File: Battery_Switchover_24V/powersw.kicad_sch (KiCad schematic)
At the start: 39 parts, among them J10 ATX_2X3, J11 ATX_2X3, J12 ATX_2X3, J13 ATX_2X3, J2 M8, J4 M8, J5 M8, J8 ATX_2X3, J9 ATX_2X3, Q10 FDBL86066-F085, Q4 FDBL86066-F085, Q5 FDBL86066-F085, Q6 FDBL86066-F085, Q7 FDBL86066-F085, Q8 FDBL86066-F085, Q9 FDBL86066-F085, U15 IRS21867S, U16 LM74610QDGKRQ1, U17 IRS21867S, U3 IRS21867S, U6 LM74610QDGKRQ1

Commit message: Board turned to horizontal
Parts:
- C9: footprint Capacitor_SMD:C_0603_1608Metric -> Capacitor_SMD:C_1206_3216Metric
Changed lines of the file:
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@@
 			)
 		)
-		(property "Footprint" "Capacitor_SMD:C_0603_1608Metric"
+		(property "Footprint" "Capacitor_SMD:C_1206_3216Metric"
 			(at 92.71 187.96 0)
 			(effects

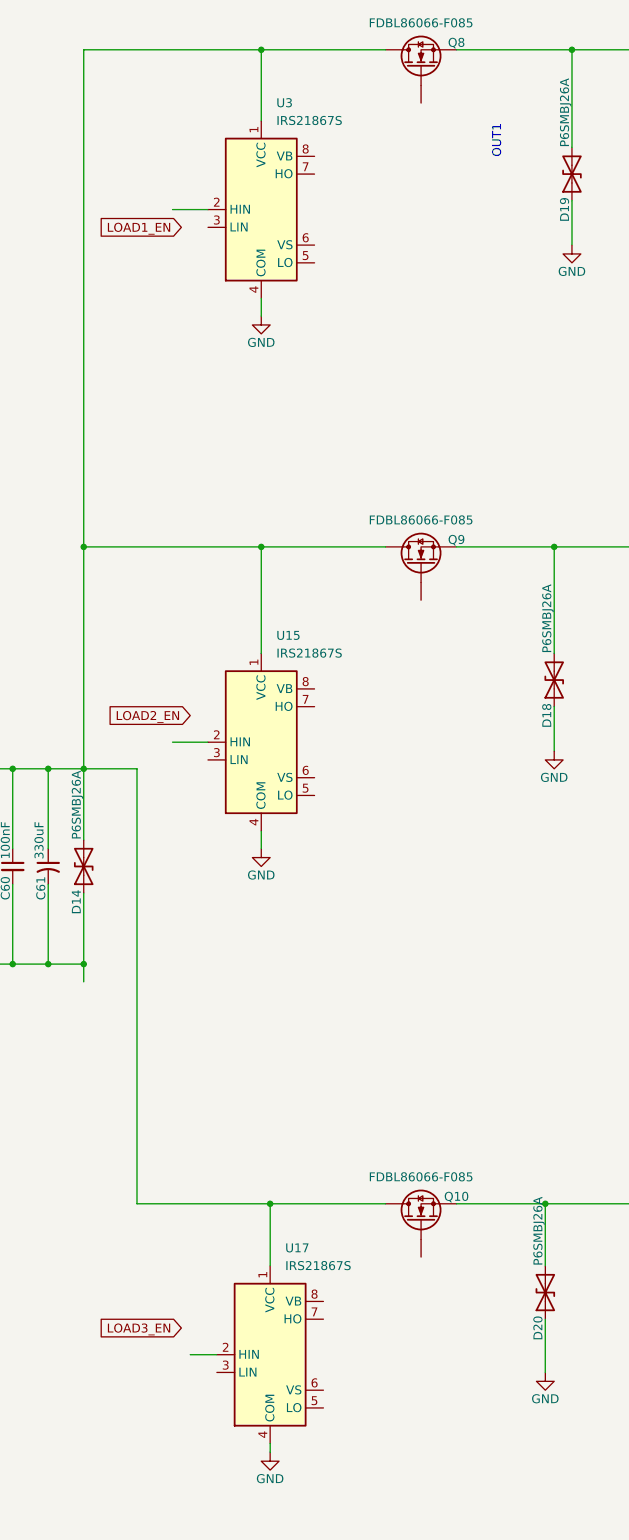
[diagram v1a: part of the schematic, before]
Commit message: hiside load switch revised
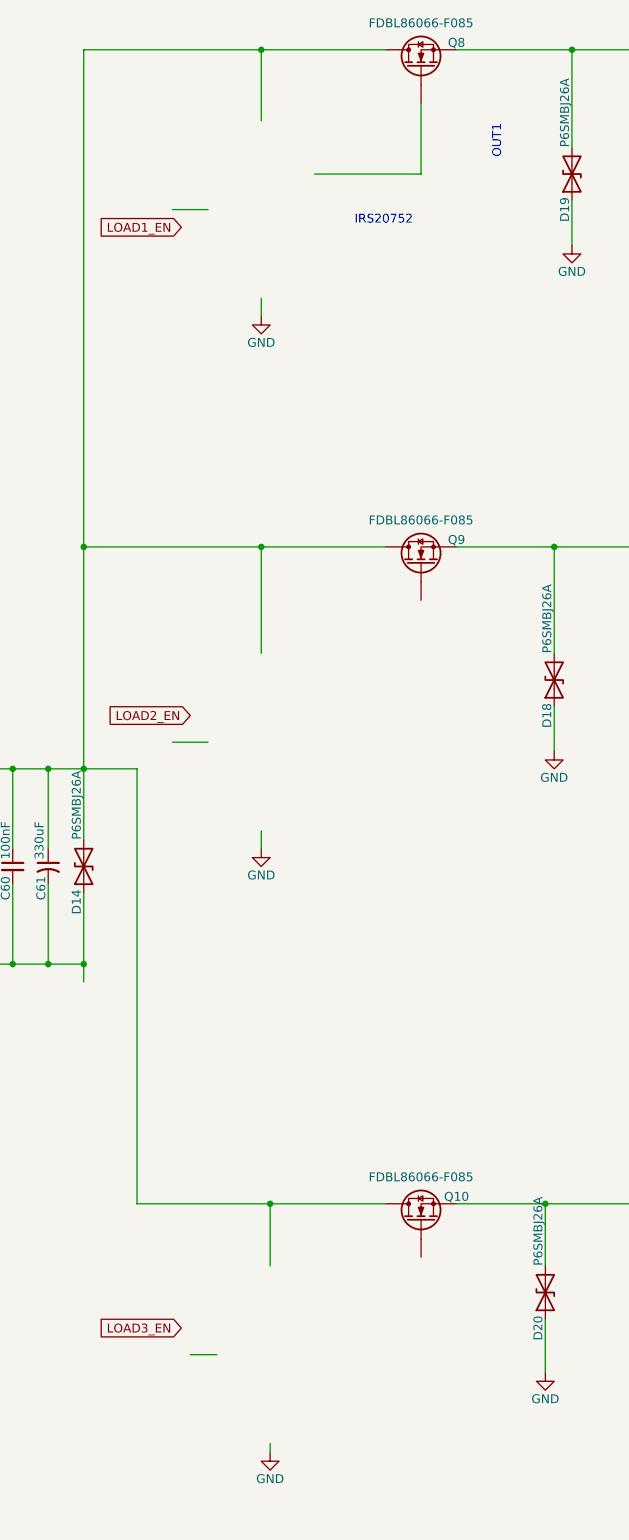
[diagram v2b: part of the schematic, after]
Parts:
- removed U15, U17, U3: IRS21867S, Package_SO:SOIC-8_3.9x4.9mm_P1.27mm, symbol Driver_FET:IRS21867S
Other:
- note added: "IRS20752"

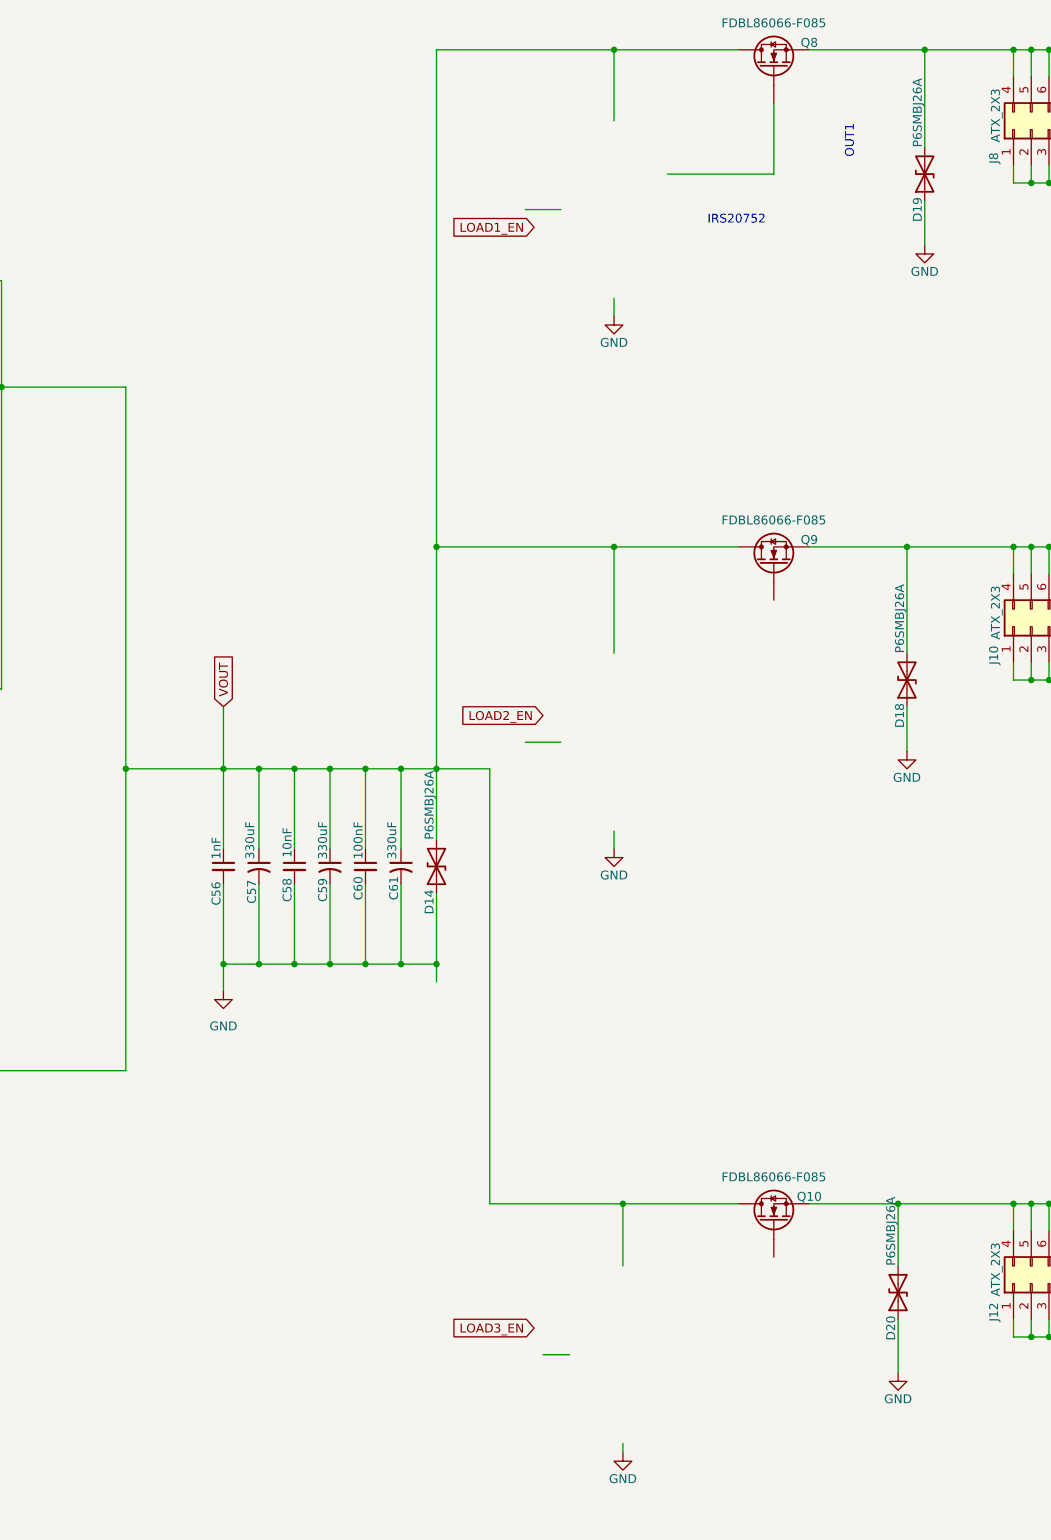
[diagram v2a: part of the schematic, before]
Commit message: Plane tracks added. Load caps placement
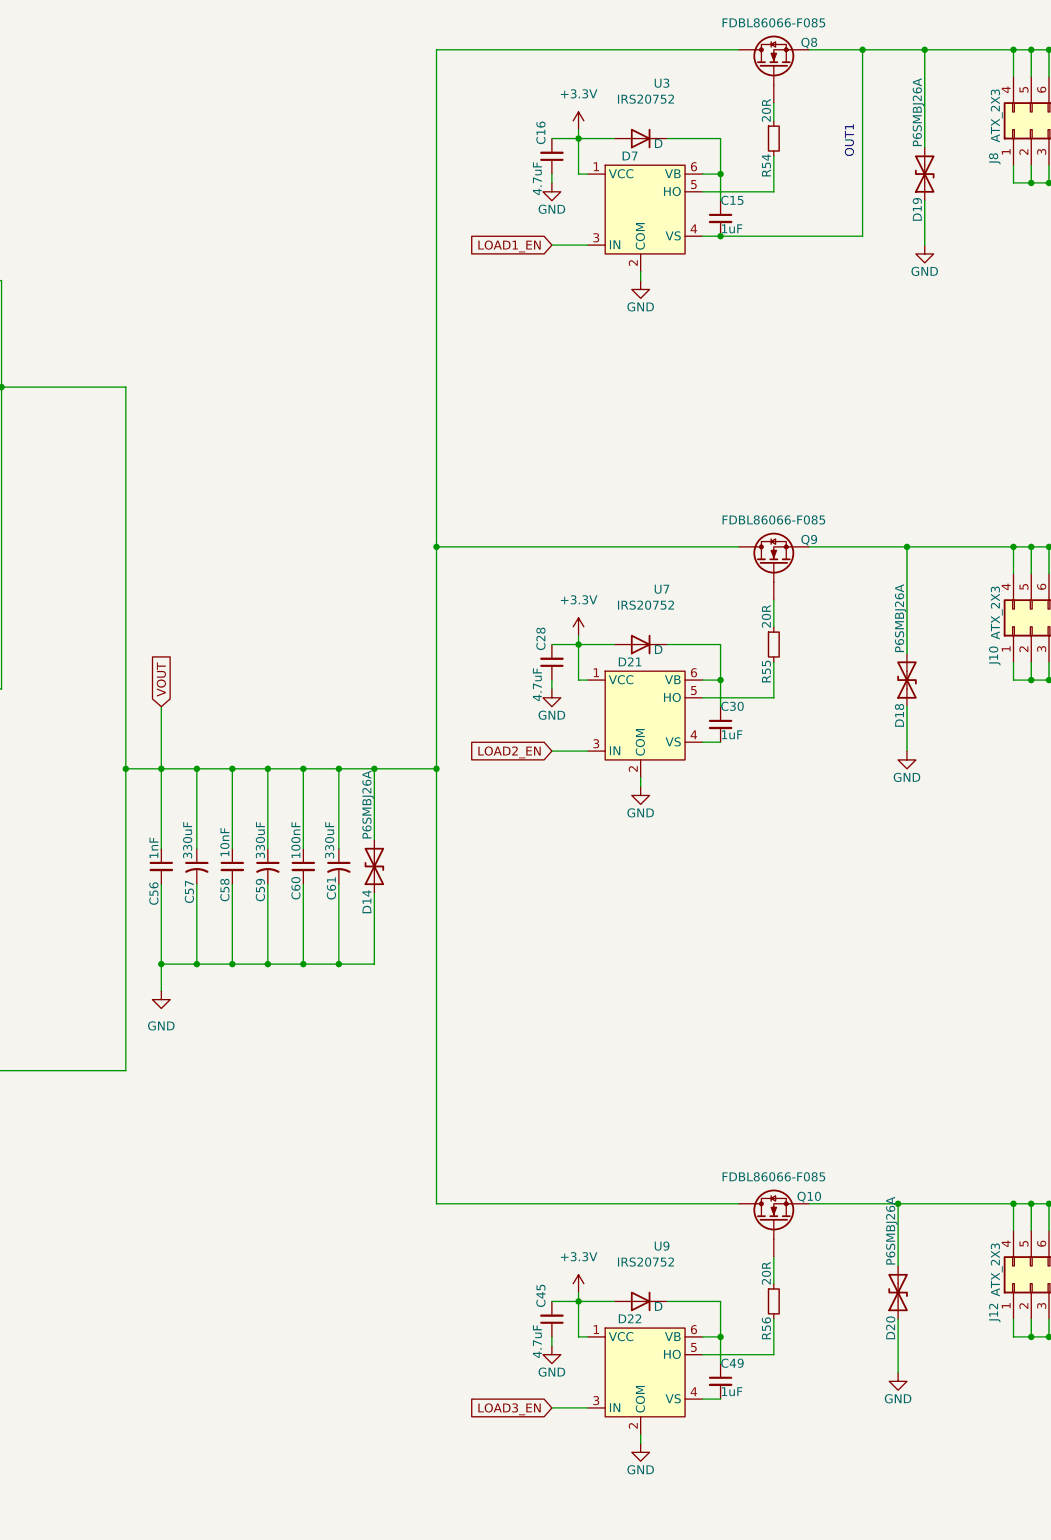
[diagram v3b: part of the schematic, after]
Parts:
- added C15, C30, C49: 1uF, Capacitor_SMD:C_0805_2012Metric, symbol Device:C_Small
- added C16, C28, C45: 4.7uF, Capacitor_SMD:C_1206_3216Metric, symbol Device:C_Small
- added D21, D22, D7: D, Diode_SMD:D_SOD-323_HandSoldering, symbol Device:D
- added R54, R55, R56: 20R, Resistor_SMD:R_0603_1608Metric, symbol Device:R_Small
- added U3, U7, U9: IRS20752, Package_TO_SOT_SMD:SOT-23-6, symbol irs20752:IRS20752
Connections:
- net GND: now also C16.1, C28.1, C45.1, U3.2 (COM), U7.2 (COM), U9.2 (COM)
- net LOAD1_EN: now also U3.3 (IN)
- net LOAD2_EN: now also U7.3 (IN)
- net LOAD3_EN: now also U9.3 (IN)
- net at Q10.1 (G): now also R56.1
- net at D19.2 (A2), J8.4 (Pin_4), J8.5 (Pin_5)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: now also C15.2, U3.4 (VS)
- net at Q9.1 (G): now also R55.1
- net at Q8.1 (G): now also R54.1
- new net: R54.2, U3.5 (HO)
- new net: C15.1, D7.1 (K), U3.6 (VB)
- new net: C30.2, U7.4 (VS)
- new net: R55.2, U7.5 (HO)
- new net: C30.1, D21.1 (K), U7.6 (VB)
- new net: C49.1, D22.1 (K), U9.6 (VB)
- new net: R56.2, U9.5 (HO)
- new net: C49.2, U9.4 (VS)
- new net +3.3V: C16.2, C28.2, C45.2, D21.2 (A), D22.2 (A), D7.2 (A), U3.1 (VCC), U7.1 (VCC), U9.1 (VCC)
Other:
- note removed: "IRS20752"
- moved on the sheet: C56, C57, C58, C59, C60, C61, D14

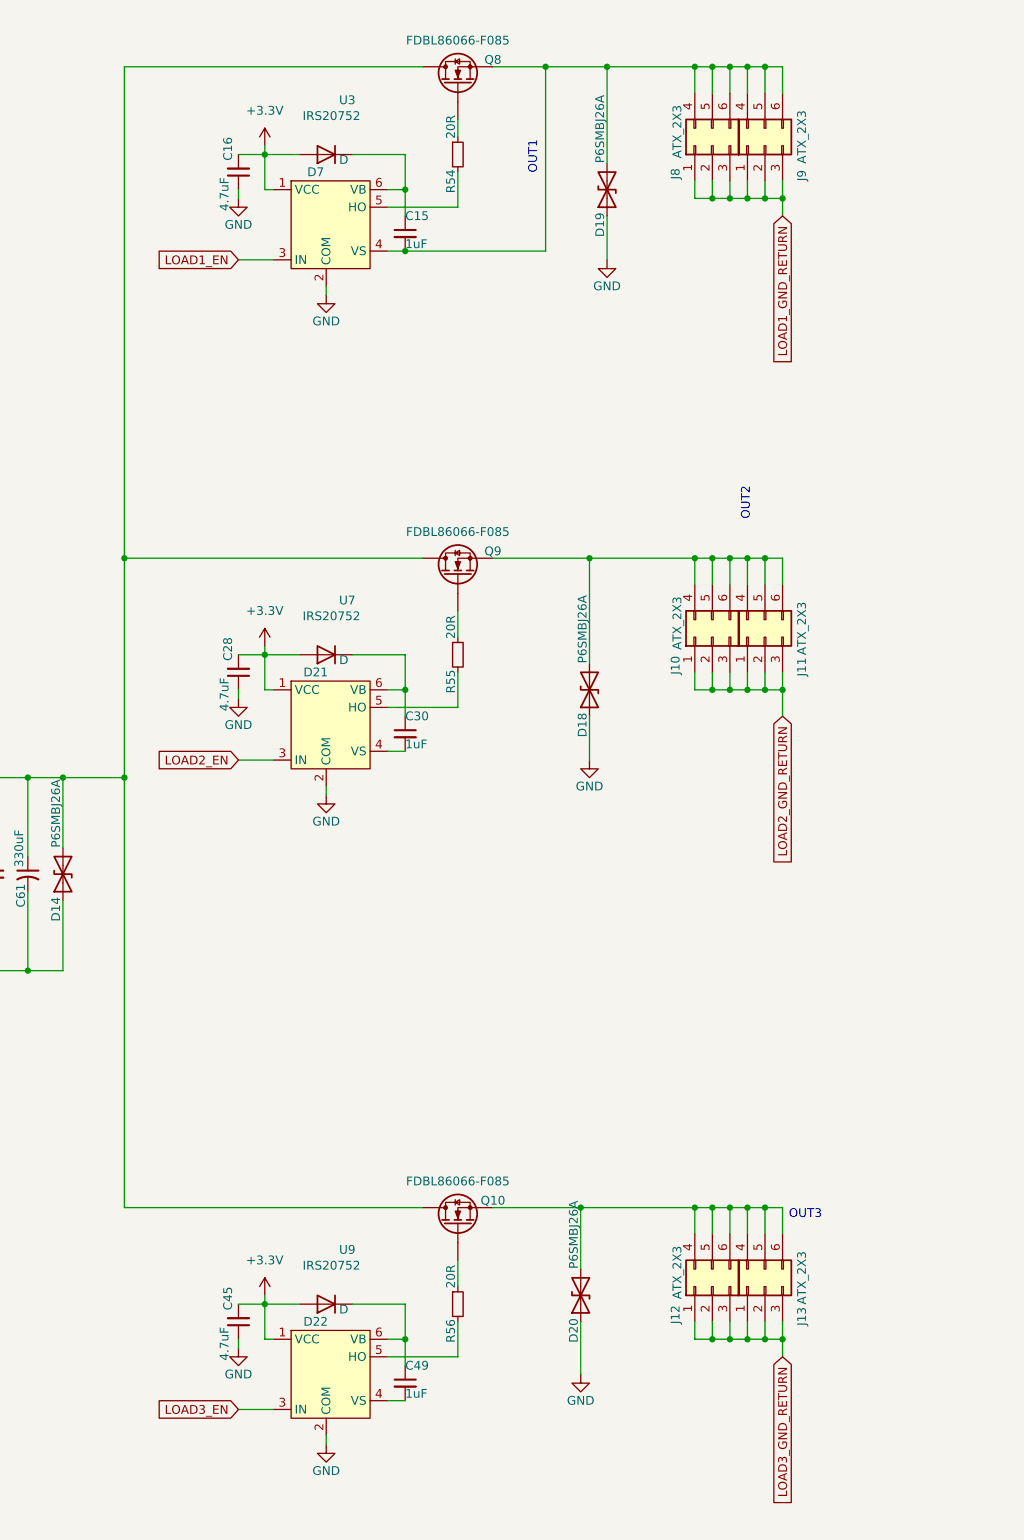
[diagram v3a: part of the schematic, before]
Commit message: Added ATX fuses
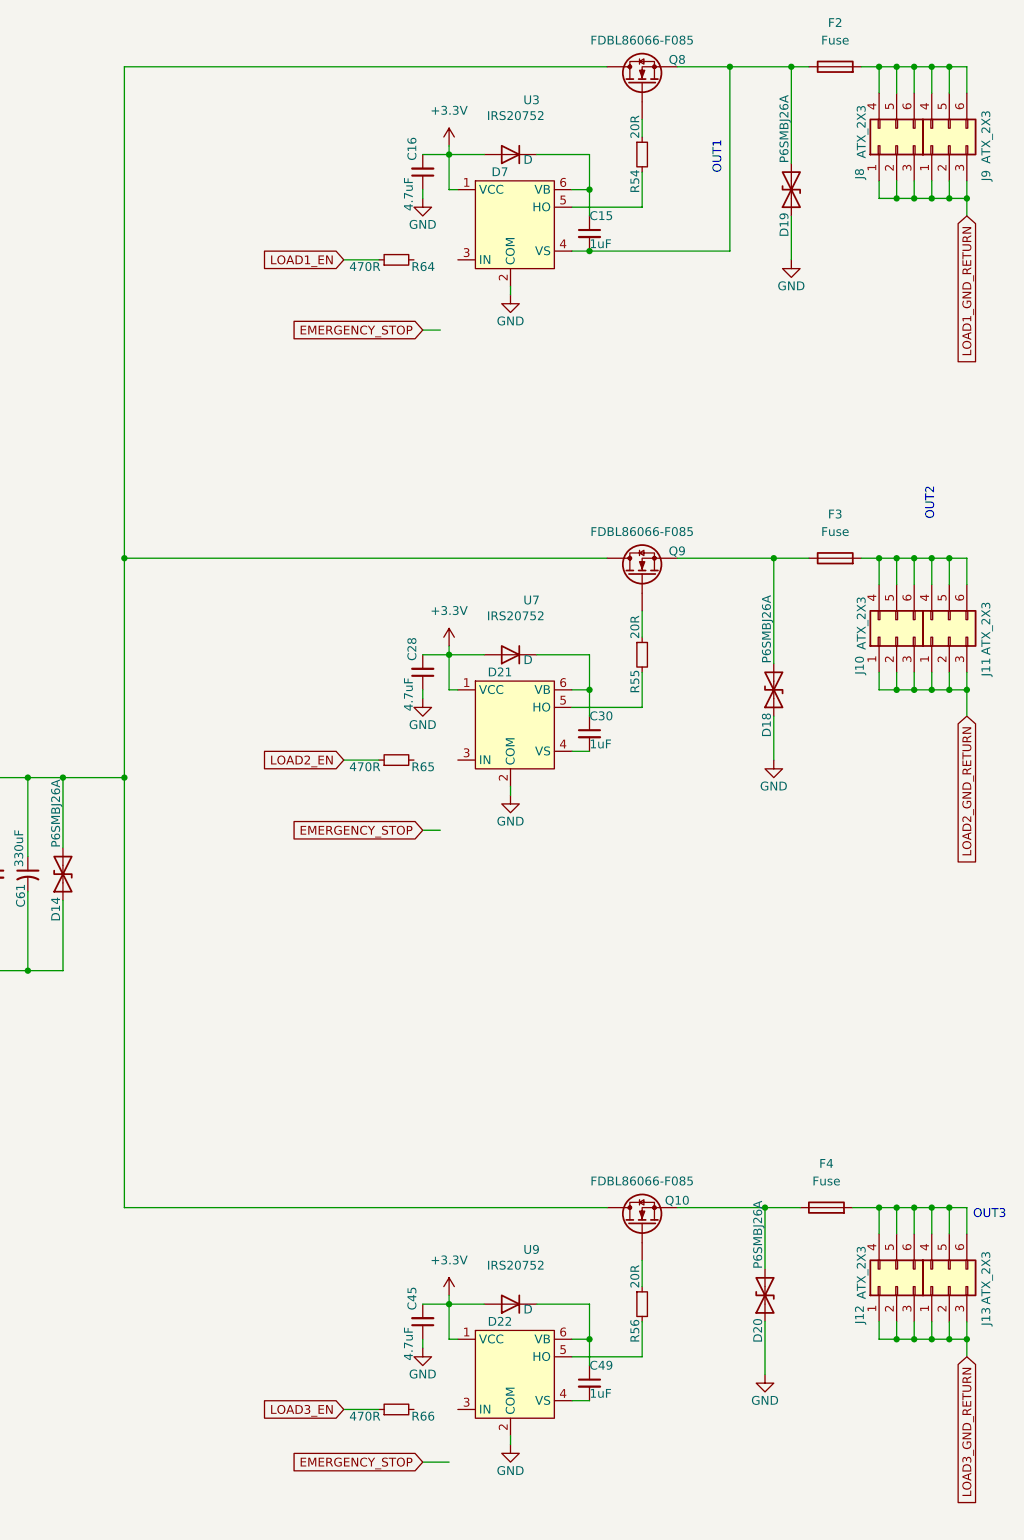
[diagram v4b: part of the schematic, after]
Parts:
- added F2, F3, F4: Fuse, Fuse:Fuseholder_Blade_Mini_Keystone_3568, symbol Device:Fuse
- added R64, R65, R66: 470R, Resistor_SMD:R_0603_1608Metric, symbol Device:R_Small
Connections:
- net LOAD1_EN: now also R64.1; no longer U3.3 (IN)
- net LOAD2_EN: now also R65.1; no longer U7.3 (IN)
- net LOAD3_EN: now also R66.1; no longer U9.3 (IN)
- net at J8.4 (Pin_4), J8.5 (Pin_5), J8.6 (Pin_6)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: now also F2.2; no longer C15.2, D19.2 (A2), Q8.2 (S), U3.4 (VS)
- net at J12.4 (Pin_4), J12.5 (Pin_5), J12.6 (Pin_6)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: now also F4.2; no longer D20.2 (A2), Q10.2 (S)
- net at J10.4 (Pin_4), J10.5 (Pin_5), J10.6 (Pin_6)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: now also F3.2; no longer D18.2 (A2), Q9.2 (S)
- new net: C15.2, D19.2 (A2), F2.1, Q8.2 (S), U3.4 (VS)
- new net: D20.2 (A2), F4.1, Q10.2 (S)
- new net: D18.2 (A2), F3.1, Q9.2 (S)
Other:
- moved on the sheet: C15, C16, C28, C30, C45, C49, D18, D19, D20, D21, D22, D7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
